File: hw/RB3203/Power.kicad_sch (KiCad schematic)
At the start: 17 parts

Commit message: Wip
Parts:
- added Q? (x2): Q_PMOS_DGS, RBCX:JMSL0302AU, symbol Device:Q_PMOS_DGS
- added U? (x2): 2N7002, Package_TO_SOT_SMD:SOT-23, symbol B.B-rescue:2N7002-Transistor_FET-B.B-rescue-B.B-rescue
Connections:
- net 5V: now also Q?.3 (S), Q?.3 (S)
- new net: Q?.2 (G), U?.1 (G) (x2)
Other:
- moved on the sheet: U?

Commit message: Two 5V brange with automatic shutdown step-up
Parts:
- removed Q?: Q_PMOS_DGS, RBCX:JMSL0302AU, symbol Device:Q_PMOS_DGS
- removed U?: 7.5k, Resistor_SMD:R_0402_1005Metric, symbol B.B-rescue:R-Device-B.B-rescue-B.B-rescue
- removed U? (x2): 2N7002, Package_TO_SOT_SMD:SOT-23, symbol B.B-rescue:2N7002-Transistor_FET-B.B-rescue-B.B-rescue
- added Q?: Q_PMOS_DGS, RBCX:JMSL0302AU, symbol Device:Q_PMOS_DGS
- added Q? (x2): PMOS-2x_BSS84DW, symbol Robotarna_KiCad_Library:PMOS-2x_BSS84DW
- added R?: 10k, Capacitor_SMD:C_0201_0603Metric, symbol Device:R
- added U? (x2): 100k, Resistor_SMD:R_0402_1005Metric, symbol B.B-rescue:R-Device-B.B-rescue-B.B-rescue
- added U? (x2): 2N7002, Package_TO_SOT_SMD:SOT-23, symbol B.B-rescue:2N7002-Transistor_FET-B.B-rescue-B.B-rescue
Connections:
- net 3V3: now also Q?.1 (S), Q?.4 (S)
- net 5V: now also Q?.3 (S), U?.1, U?.1
- net GND: now also R?.1, U?.2 (S), U?.2 (S)
- net at Q?.2 (G): now also U?.2, U?.3 (D)
- net 5V-A: now reaches Q?.1 (D)
- net SHUTDOWN_5V: no longer names the net of U?.1 (G)
- net SHUTDOWN_5V: now also Q?.3 (D), Q?.6 (D), R?.2
- new net: Q?.2 (G), U?.2, U?.3 (D)
- new net 5V-B: Q?.1 (D)
- new net EN-5V-A: Q?.2 (G), U?.1 (G)
- new net EN-5V-B: Q?.5 (G), U?.1 (G)
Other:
- moved on the sheet: Q?, U?

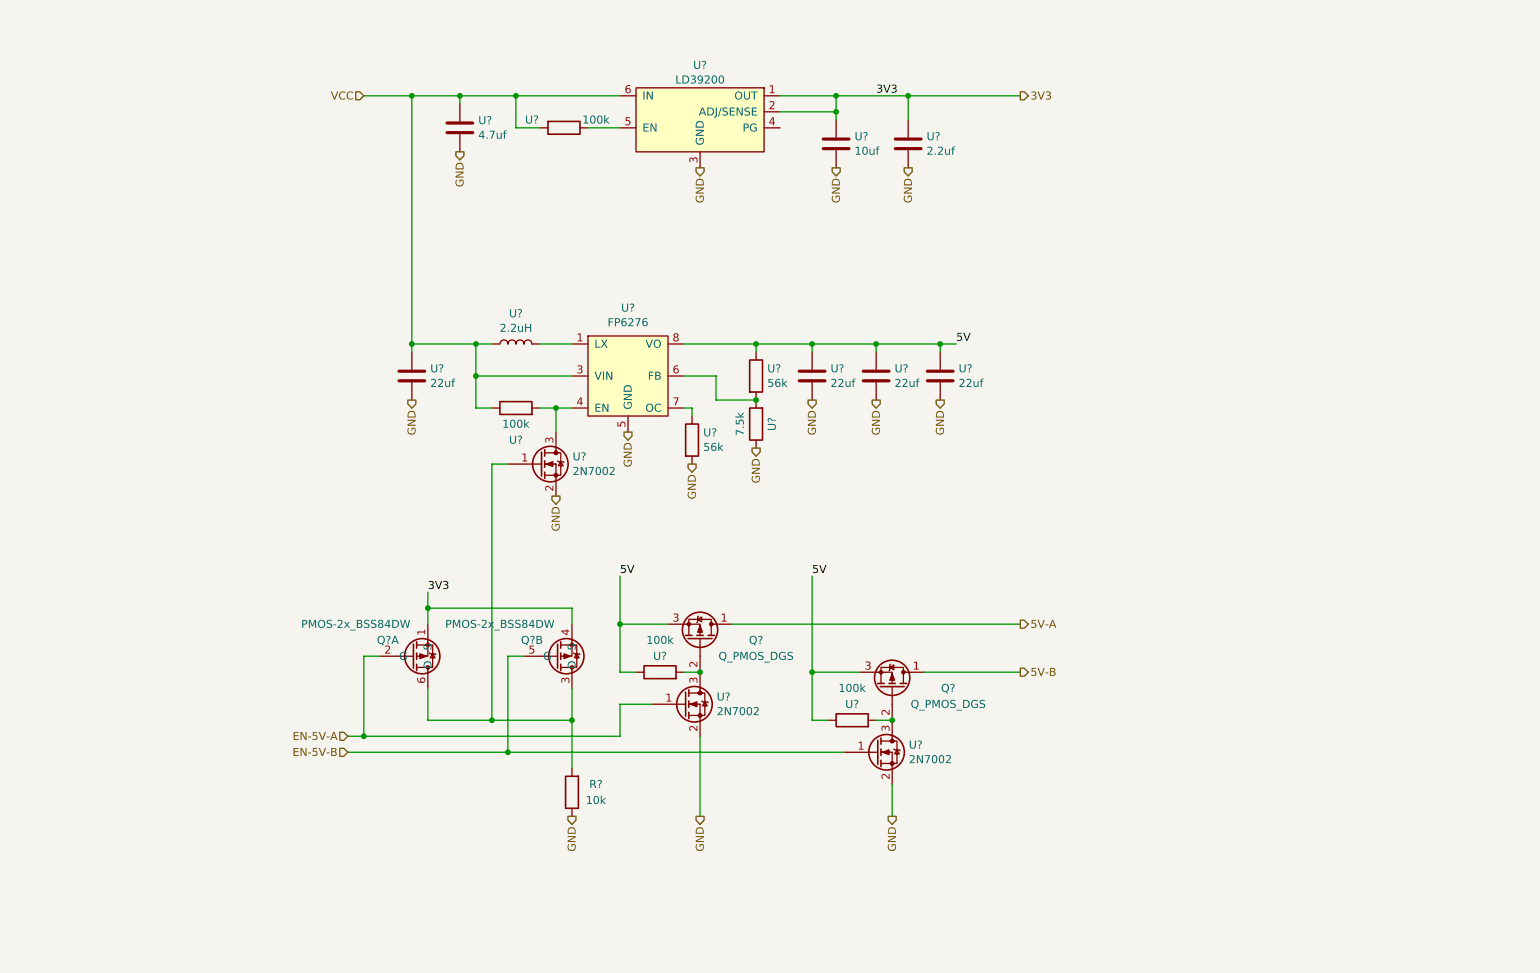
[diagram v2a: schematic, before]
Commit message: Simplify of automatic shutdown step-up
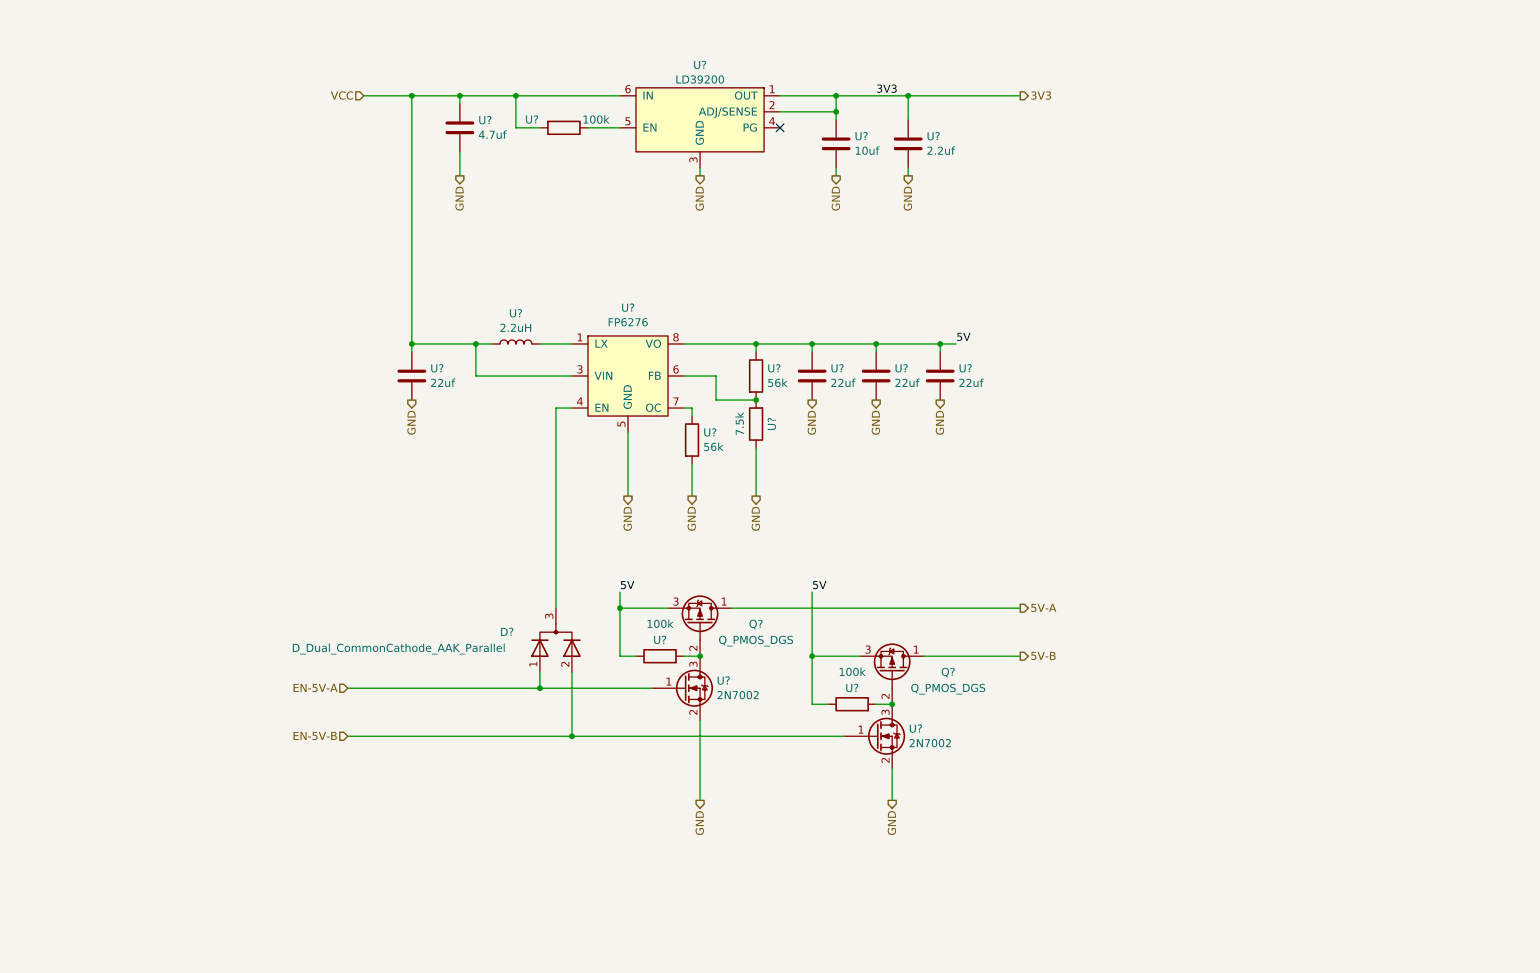
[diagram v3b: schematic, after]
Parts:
- removed Q? (x2): PMOS-2x_BSS84DW, symbol Robotarna_KiCad_Library:PMOS-2x_BSS84DW
- removed R?: 10k, Capacitor_SMD:C_0201_0603Metric, symbol Device:R
- removed U?: 100k, Resistor_SMD:R_0402_1005Metric, symbol B.B-rescue:R-Device-B.B-rescue-B.B-rescue
- removed U?: 2N7002, Package_TO_SOT_SMD:SOT-23, symbol B.B-rescue:2N7002-Transistor_FET-B.B-rescue-B.B-rescue
- added D?: D_Dual_CommonCathode_AAK_Parallel, Package_TO_SOT_SMD:SOT-723, symbol Device:D_Dual_CommonCathode_AAK_Parallel
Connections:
- net EN-5V-A: now also D?.1 (K)
- net EN-5V-B: now also D?.2 (K)
- net at U?.4 (EN): now also D?.3 (A)
- no-connect marks 0 -> 1
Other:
- moved on the sheet: Q?, U?

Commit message: Wip
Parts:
- removed U?: FP6276, Package_SO:SOIC-8-1EP_3.9x4.9mm_P1.27mm_EP2.41x3.81mm_ThermalVias, symbol B.B-rescue:FP6276-B.B-rescue-B.B-rescue
- added U? (x2): 100n, Capacitor_SMD:C_0402_1005Metric, symbol B.B-rescue:C-Device-B.B-rescue-B.B-rescue
- added U?: TPS61088RHLR, RHL0020A, symbol Robotarna_KiCad_Library:TPS61088RHLR
- added U?: 150k, Resistor_SMD:R_0402_1005Metric, symbol B.B-rescue:R-Device-B.B-rescue-B.B-rescue
- added U?: 10uf, Capacitor_SMD:C_0805_2012Metric, symbol B.B-rescue:C-Device-B.B-rescue-B.B-rescue
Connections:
- net GND: now also U?.2, U?.2
- net VCC: now also U?.1, U?.1, U?.9 (VIN)
- net LX renamed SW
- net SW: now also U?.1, U?.1, U?.4 (SW), U?.5 (SW), U?.6 (SW), U?.7 (SW)
- new net: U?.2, U?.8 (BOOT)
- new net: U?.14 (VOUT), U?.15 (VOUT), U?.16 (VOUT)
- new net: U?.2, U?.3 (FSW)
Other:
- note added: "Step-UP:"
- note added: "Switching freqvenci = 1 017 kHz"
- moved on the sheet: D?, Q?, U?

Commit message: Wip
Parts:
- removed U?: 22uf, Capacitor_SMD:C_0805_2012Metric, symbol B.B-rescue:C-Device-B.B-rescue-B.B-rescue
- added C?: 1u, Capacitor_SMD:C_0402_1005Metric, symbol Device:C
- added U?: 22u, Capacitor_SMD:C_0805_2012Metric, symbol B.B-rescue:C-Device-B.B-rescue-B.B-rescue
- U? (x3): value 22uf -> 22u
- U?: value 4.7uf -> 4.7u
- U?: value 2.2uH -> 2.2u
- U?: value 2.2uf -> 2.2u
- U?: value 7.5k -> 17.4k; LCSC C25918 -> C226818
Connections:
- net 5V: now also U?.14 (VOUT), U?.15 (VOUT), U?.16 (VOUT), C?.1, U?.1
- net GND: now also U?.11 (NC), U?.12 (NC), U?.20 (AGND), U?.21 (PGND), C?.2, U?.2
- net at U?.17 (FB): now also U?.2, U?.2
- net at U?.2 (EN): now also D?.3 (A)
- no-connect marks 1 -> 2
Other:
- note added: "Switching freqvenci = 1 MHz"
- note removed: "Switching freqvenci = 1 017 kHz"
- moved on the sheet: U?

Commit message: 5V branch
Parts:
- added U?: 3.92k, Resistor_SMD:R_0402_1005Metric, symbol B.B-rescue:R-Device-B.B-rescue-B.B-rescue
- added U?: 10n, Capacitor_SMD:C_0402_1005Metric, symbol B.B-rescue:C-Device-B.B-rescue-B.B-rescue
- added U?: 100p, Capacitor_SMD:C_0402_1005Metric, symbol B.B-rescue:C-Device-B.B-rescue-B.B-rescue
- added U?: 4.7u, Capacitor_SMD:C_0805_2012Metric, symbol B.B-rescue:C-Device-B.B-rescue-B.B-rescue
- added U?: 33n, Capacitor_SMD:C_0402_1005Metric, symbol B.B-rescue:C-Device-B.B-rescue-B.B-rescue
- U?: value 56k -> 150k; LCSC C25796 -> C25755
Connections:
- net GND: now also U?.2, U?.2, U?.2, U?.2
- net at U?.1 (VCC): now also U?.1
- net at U?.10 (SS): now also U?.1
- net at U?.18 (COMP): now also U?.1, U?.1
- net at U?.19 (ILIM): now also U?.1
- new net: U?.1, U?.2
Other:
- moved on the sheet: U?

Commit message: Wip
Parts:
- U?: value 2.2u -> 1.2u; LCSC C351096 -> C2453293
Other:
- note added: "LDO"
- note added: "Switching freqvenci 1 MHz Current limit 8 A Soft start 8 ms"
- note removed: "Switching freqvenci = 1 MHz"
- moved on the sheet: C?, D?, Q?, U?
